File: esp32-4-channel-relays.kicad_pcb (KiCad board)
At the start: 2 copper layers, 59 parts, among them J1 Relay-1, J2 Relay-2, J3 Relay-3, J4 Relay-4, K1 SRD-05VDC-SL-C, K2 SRD-05VDC-SL-C, K3 SRD-05VDC-SL-C, K4 SRD-05VDC-SL-C, Q1 MBT3904DW1, Q2 BC547A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

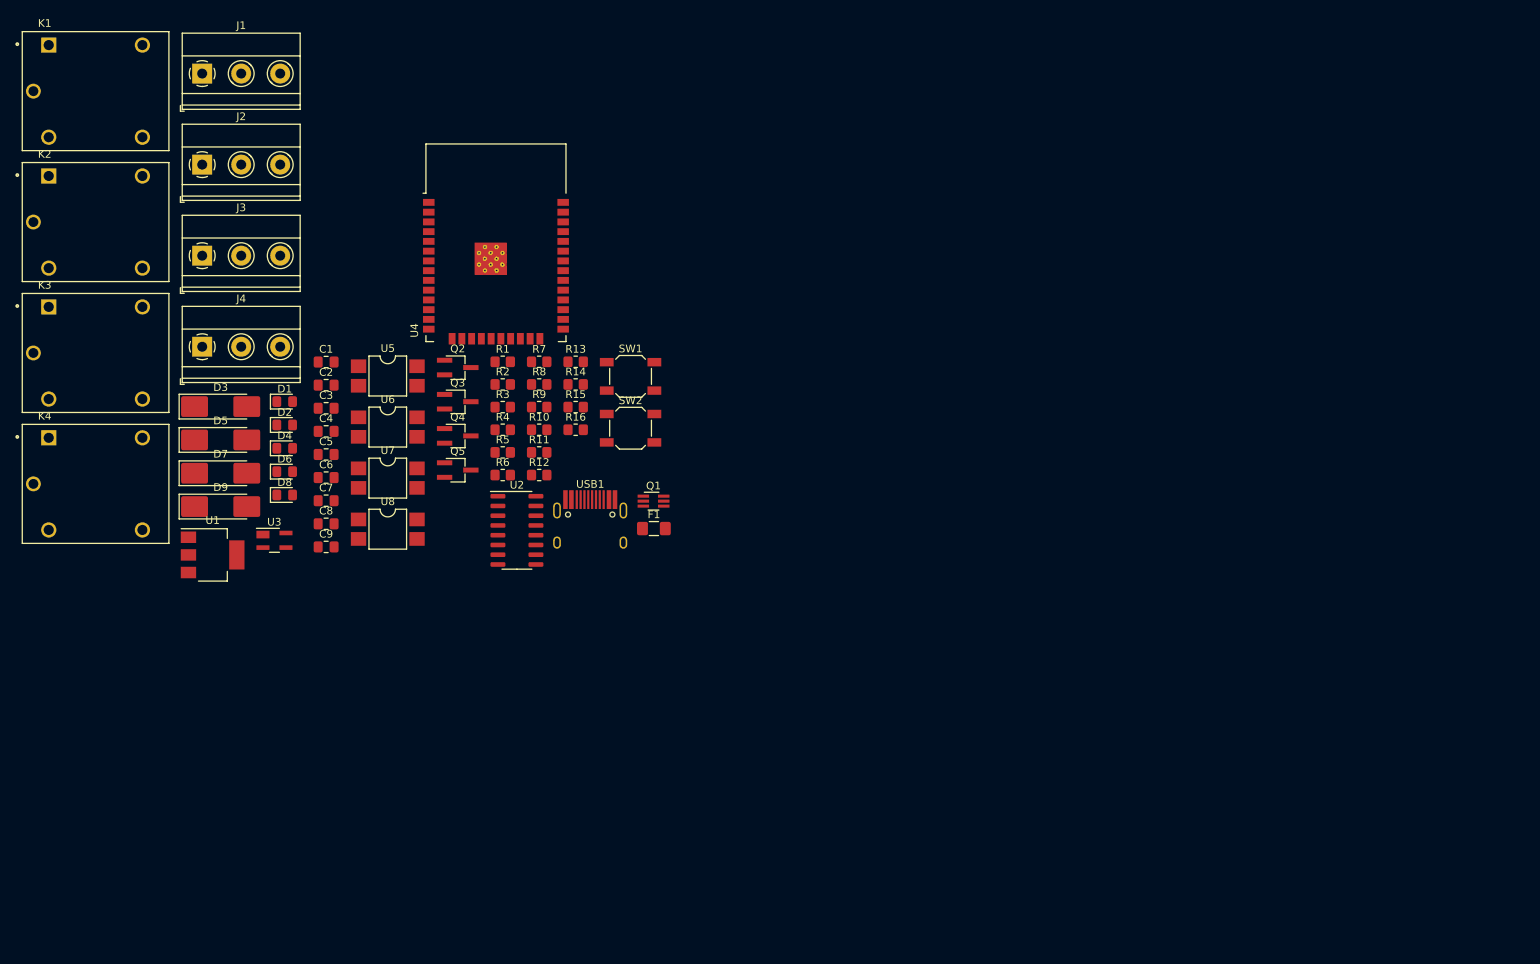
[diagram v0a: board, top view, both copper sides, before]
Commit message: Make temporary edge cut and relays placement
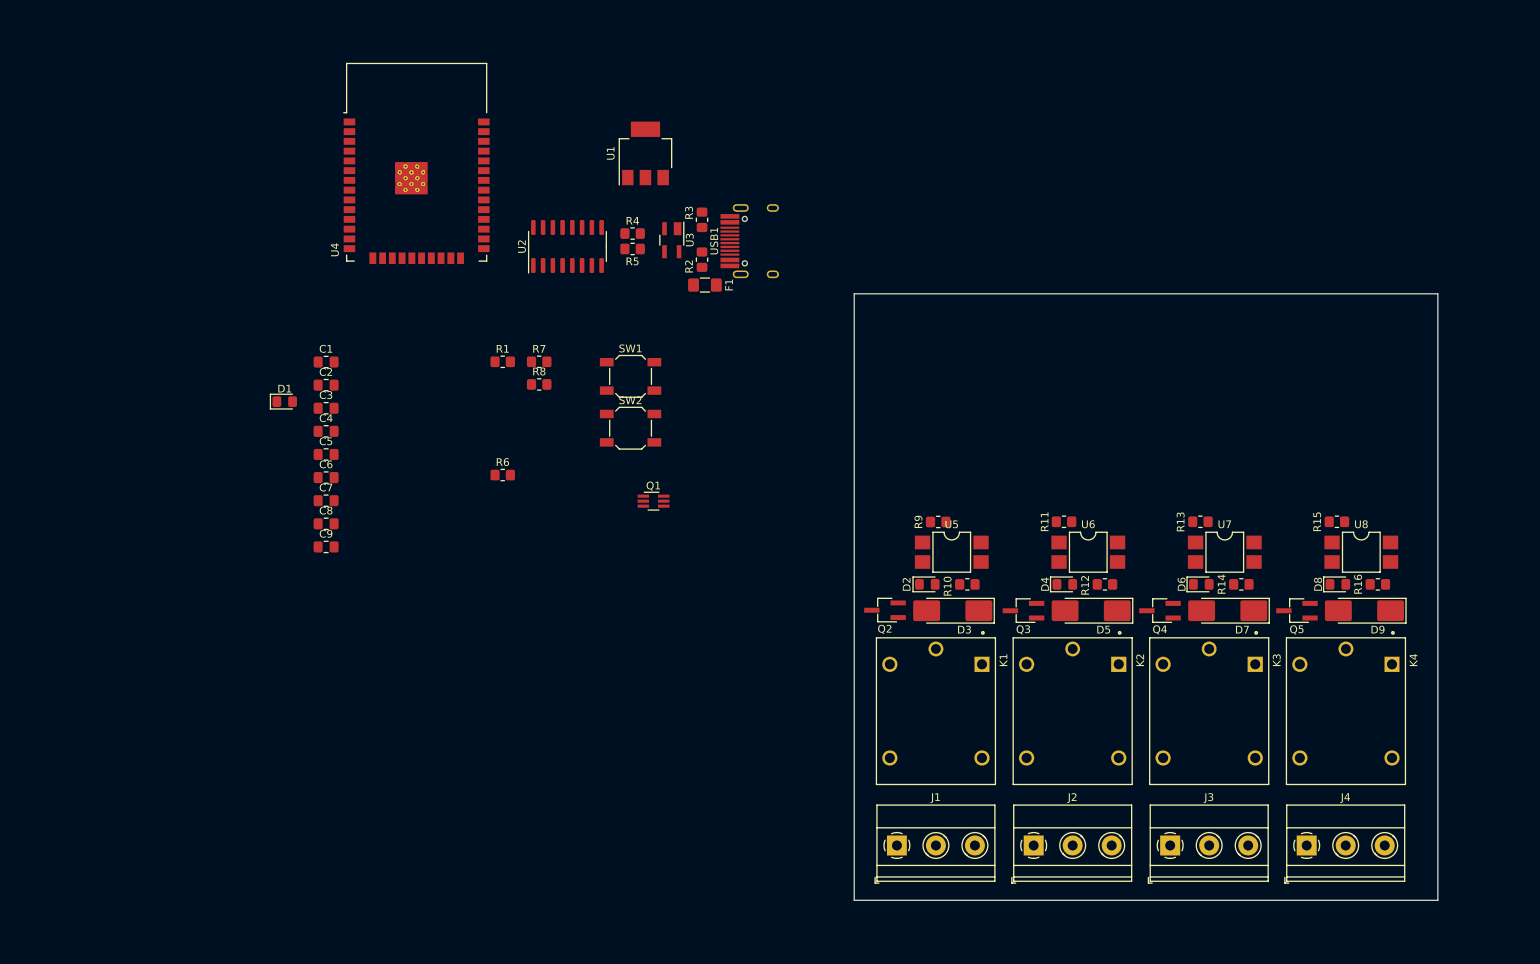
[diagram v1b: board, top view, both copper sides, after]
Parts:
- moved K4 165.5 mm to (191.0, 105.5), turned to -90 degrees
- moved J4 157.8 mm to (185.9, 123.0)
- moved K3 152.4 mm to (173.2, 105.5), turned to -90 degrees
- moved D9 149.6 mm to (193.4, 92.5), turned to 180 degrees
- moved J3 147.6 mm to (168.1, 123.0)
- moved K2 142.3 mm to (155.4, 105.5), turned to -90 degrees
- moved J2 140.0 mm to (150.4, 123.0)
- moved D8 137.7 mm to (190.0, 89.0)
- moved K1 136.0 mm to (137.6, 105.5), turned to -90 degrees
- moved J1 135.3 mm to (132.6, 123.0)
- moved D7 132.4 mm to (175.6, 92.5), turned to 180 degrees
- moved U8 126.8 mm to (193.0, 84.8)
- moved D6 120.3 mm to (172.2, 89.0)
- moved D5 115.5 mm to (157.9, 92.5), turned to 180 degrees
- moved Q5 110.8 mm to (184.7, 92.5), turned to 180 degrees
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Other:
- board outline added: 76 x 79 mm

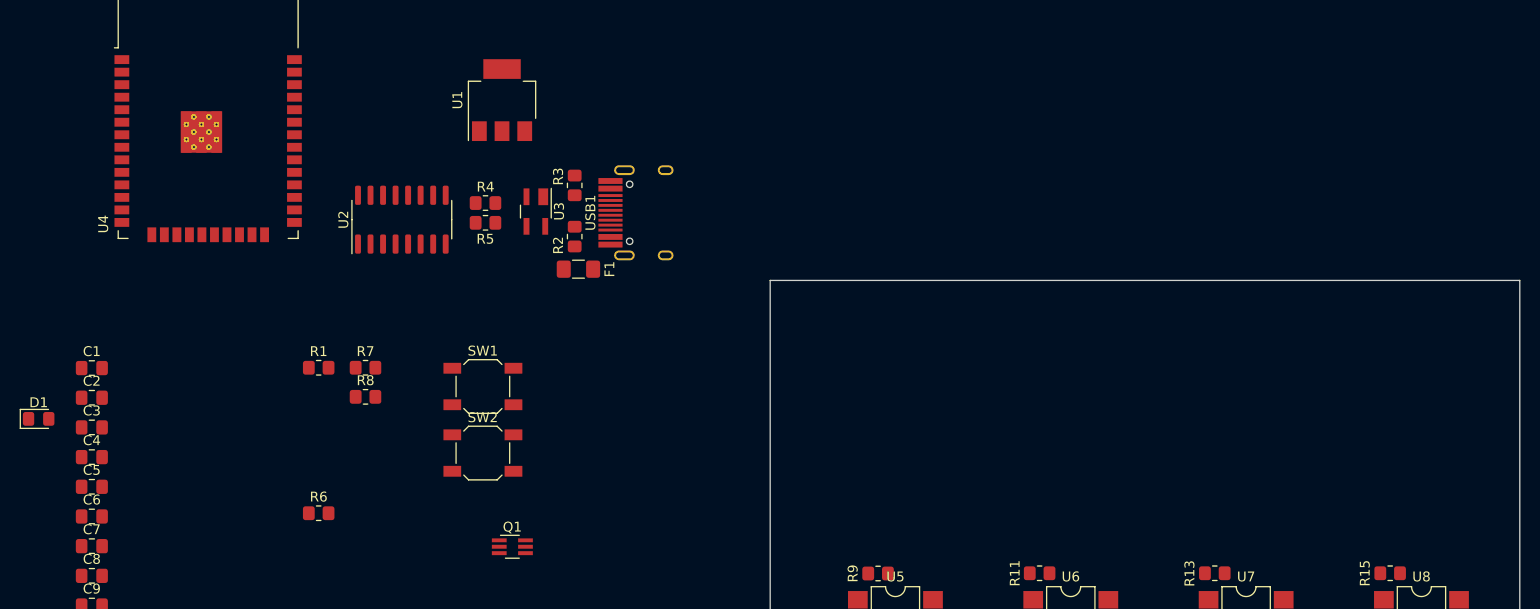
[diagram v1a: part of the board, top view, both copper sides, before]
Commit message: USB Type-C and Voltage regulator 3.3V placement
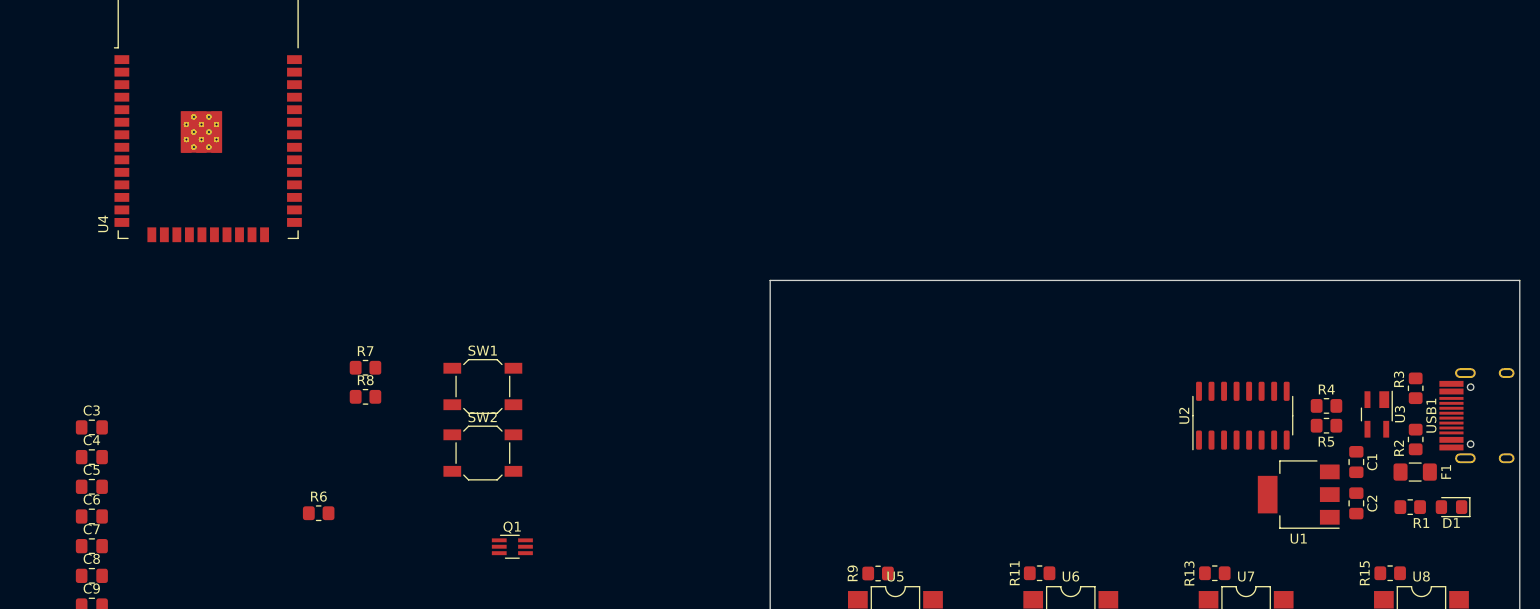
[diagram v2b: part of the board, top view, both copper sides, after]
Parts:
- moved D1 143.5 mm to (196.1, 74.2), turned to 180 degrees
- moved C2 128.7 mm to (186.4, 73.8), turned to -90 degrees
- moved C1 128.6 mm to (186.4, 69.6), turned to 90 degrees
- moved R1 111.6 mm to (191.9, 74.2)
- moved U1 90.1 mm to (180.6, 72.9), turned to 180 degrees
- moved R4 87.7 mm to (183.4, 63.9)
- moved R5 87.7 mm to (183.4, 65.9)
- moved USB1 87.7 mm to (204.3, 64.9)
- moved R2 87.7 mm to (192.5, 67.3)
- moved R3 87.7 mm to (192.5, 62.1)
- moved U3 87.7 mm to (188.5, 64.8)
- moved U2 87.6 mm to (174.9, 64.9)
- moved F1 87.3 mm to (192.4, 70.6)

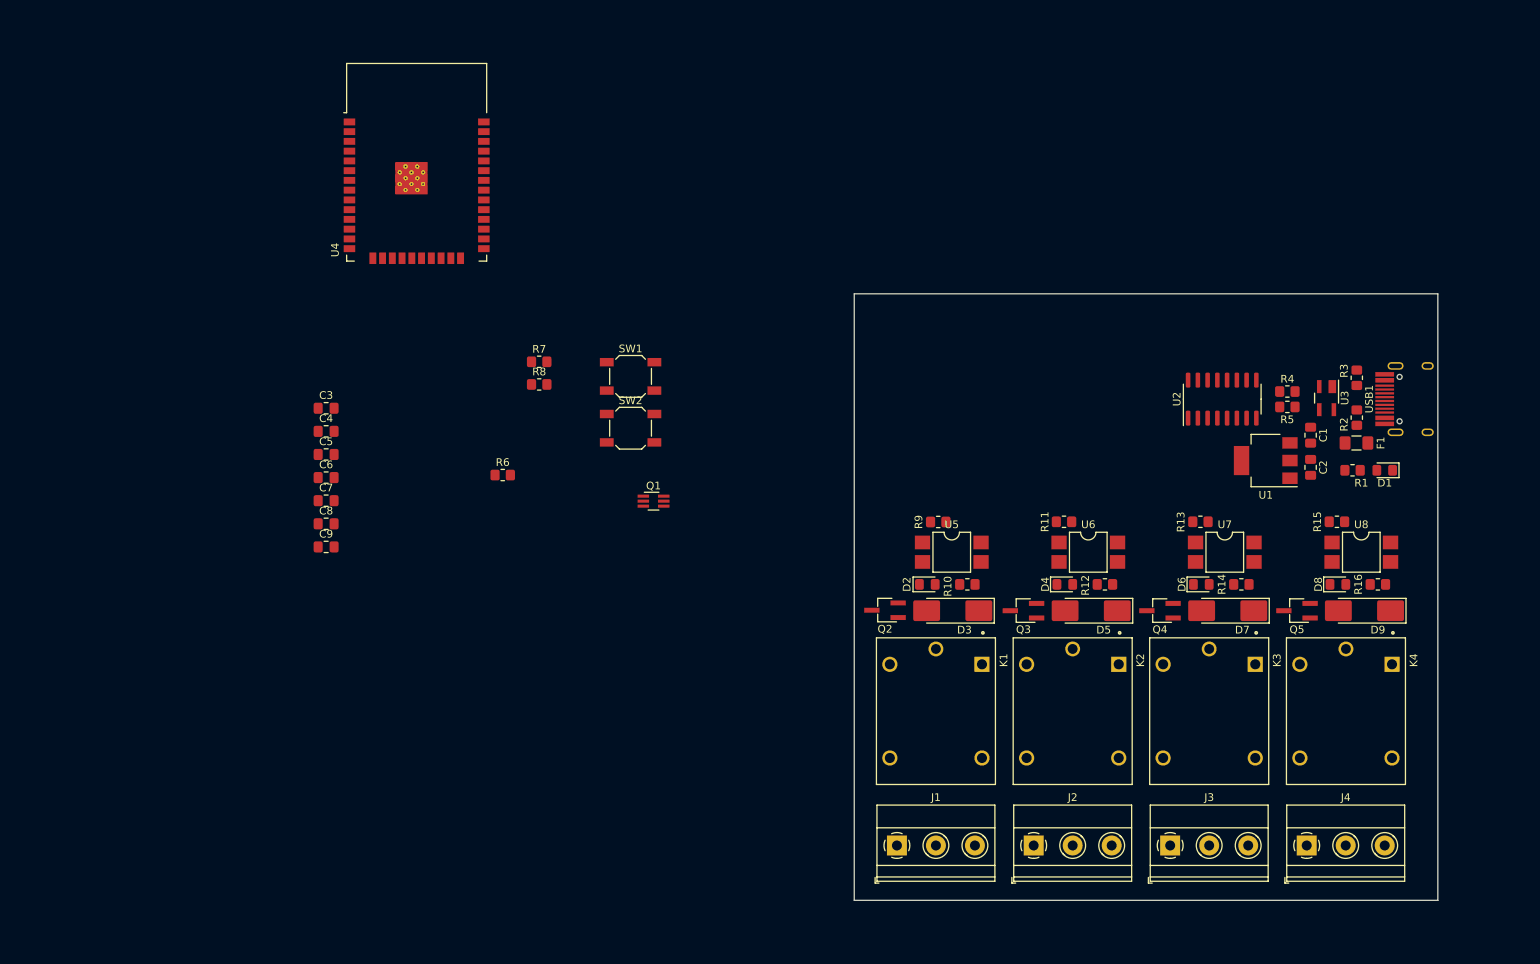
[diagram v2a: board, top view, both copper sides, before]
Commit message: ESP32, auto-reset and buttons placement also a little tweak to USB to serial converter placement
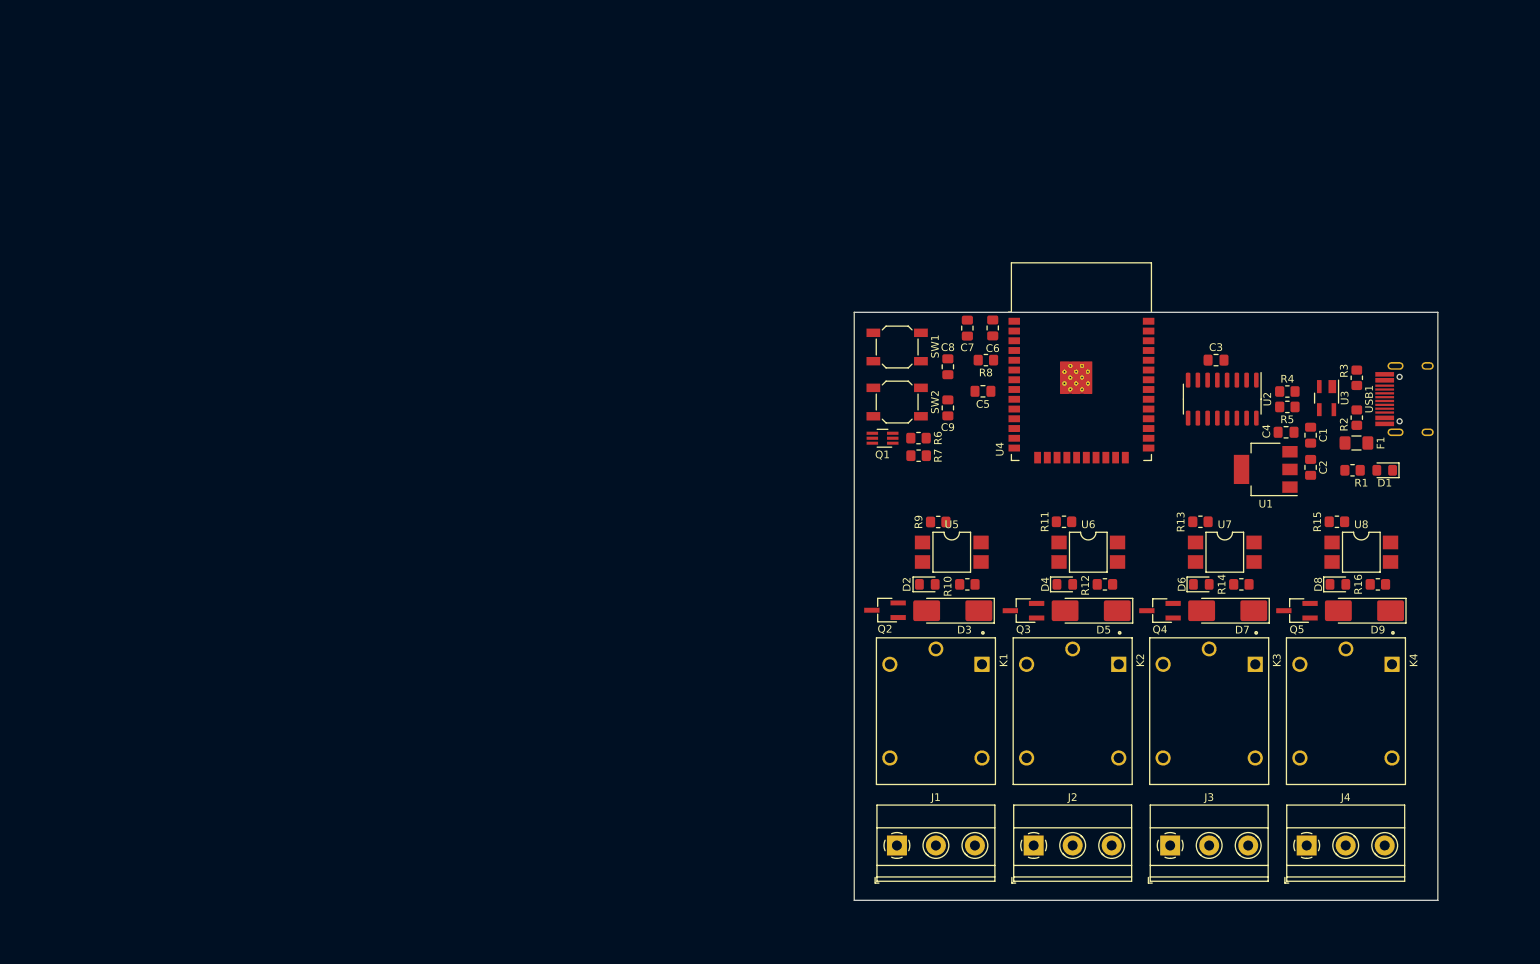
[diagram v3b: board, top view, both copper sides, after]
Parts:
- moved C4 125.0 mm to (183.2, 69.2), turned to 180 degrees
- moved C3 116.1 mm to (174.1, 59.8), turned to 180 degrees
- moved U4 90.4 mm to (156.6, 63.0)
- moved C6 89.0 mm to (145.0, 55.6), turned to 90 degrees
- moved C7 86.5 mm to (141.7, 55.6), turned to 90 degrees
- moved C5 85.9 mm to (143.8, 63.9), turned to 180 degrees
- moved C8 83.5 mm to (139.2, 60.7), turned to 90 degrees
- moved C9 83.0 mm to (139.2, 66.0), turned to -90 degrees
- moved R8 58.3 mm to (144.1, 59.8)
- moved R6 54.4 mm to (135.4, 70.0), turned to 180 degrees
- moved R7 50.9 mm to (135.4, 72.3)
- moved SW1 34.9 mm to (132.6, 58.1), turned to 180 degrees
- moved SW2 34.9 mm to (132.6, 65.3), turned to 180 degrees
- moved Q1 30.9 mm to (130.7, 70.0), turned to 180 degrees
- moved U1 1.16 mm to (180.6, 74.1)
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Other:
- board size 76 x 79 mm -> 76 x 76.6 mm
